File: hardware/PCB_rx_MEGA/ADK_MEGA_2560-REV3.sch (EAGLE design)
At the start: 9 parts

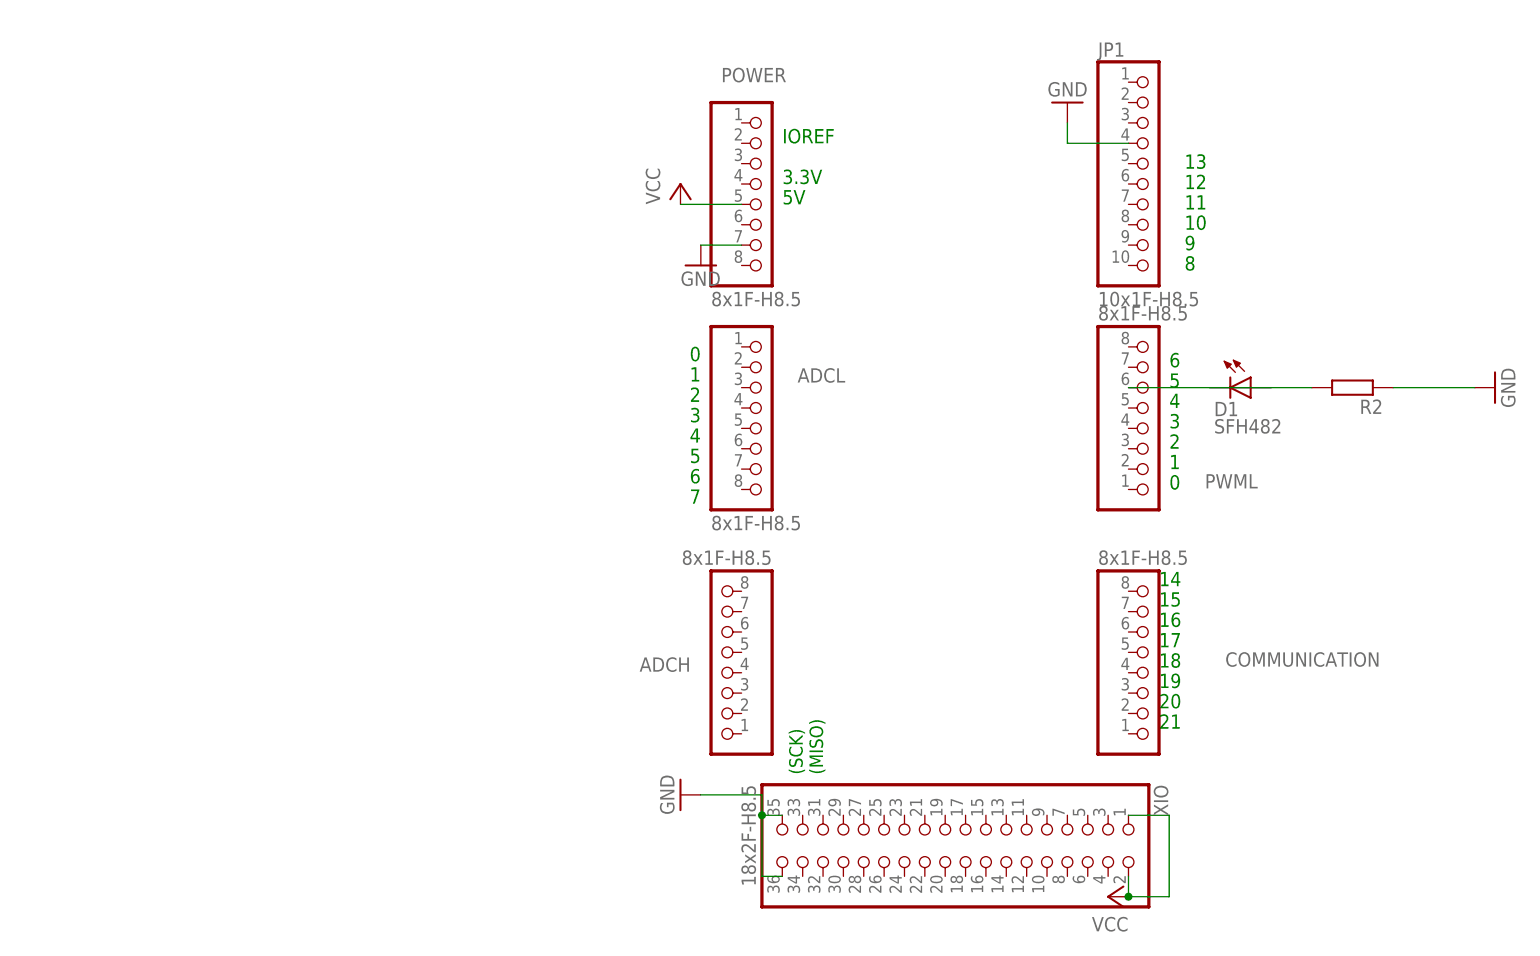
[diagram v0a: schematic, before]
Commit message: Se añade modulo de comunicaciones junto con regulador al diseño de la shield para el nodo central
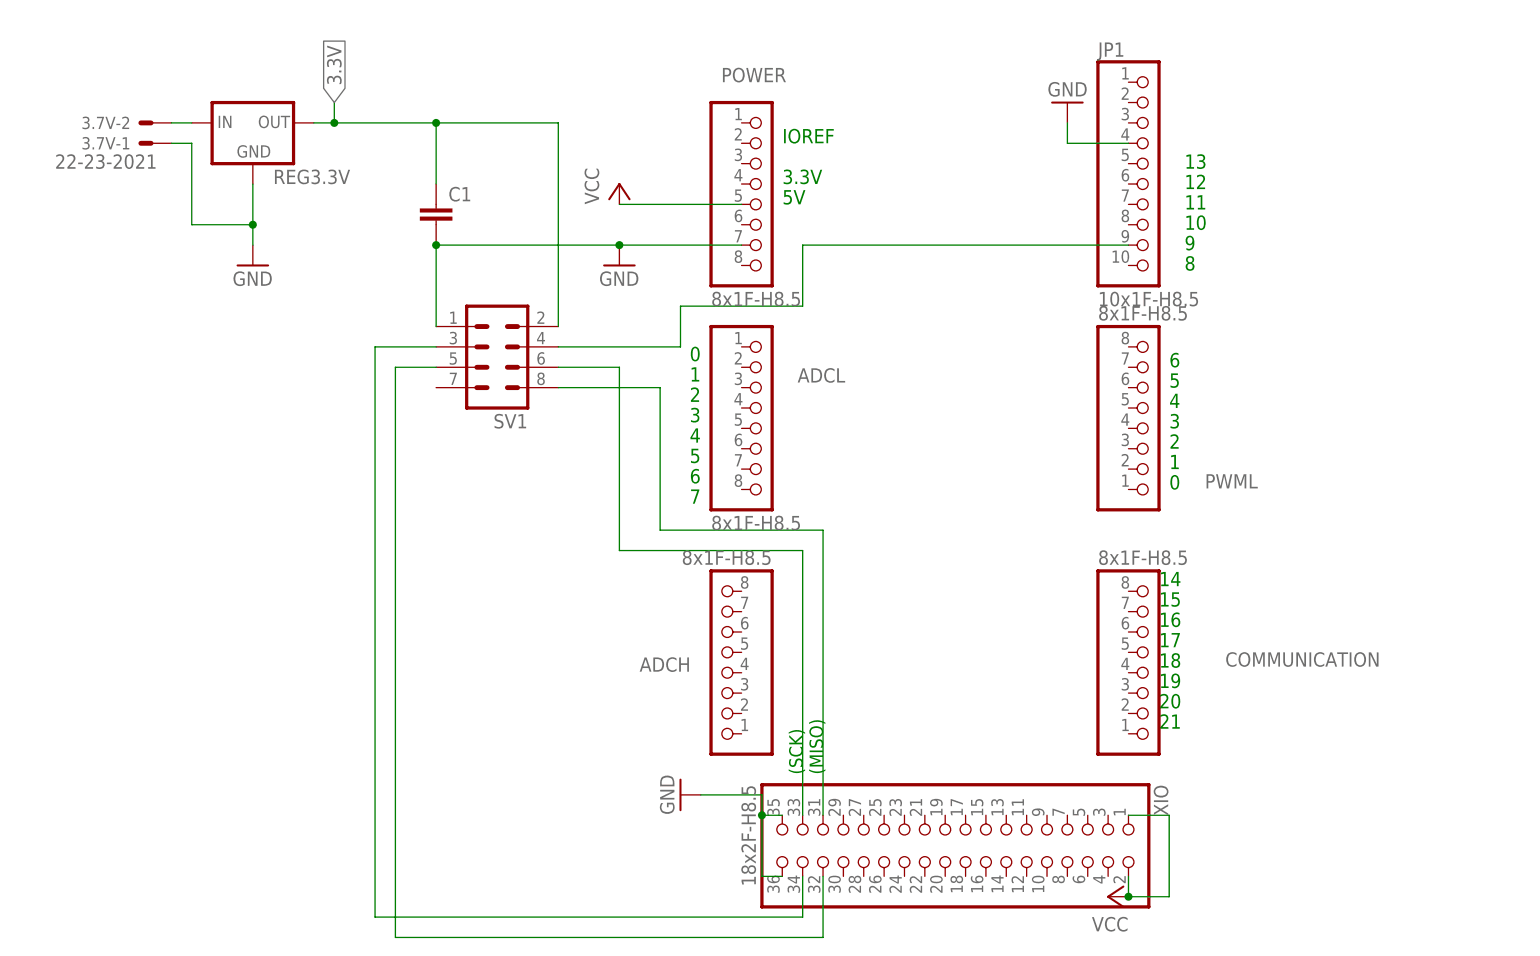
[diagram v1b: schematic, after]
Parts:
- removed D1: SFH482, led:SFH482
- removed R2: (no value), eagle-ltspice:R0204/7
- added 3.7V: 22-23-2021, con-molex:22-23-2021
- added C1: (no value), rcl:C-EU025-025X050
- added REG3.3V: (no value), v-reg:78XXL
- added SV1: (no value), con-lstb:MA04-2
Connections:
- removed net N$2: D1.C, PWML.6
- removed net N$3: D1.A, R2.2
- new net 3.3V: C1.1, REG3.3V.OUT, SV1.2
- new net N$1: SV1.3, XIO.34
- new net N$5: SV1.5, XIO.32
- new net N$6: JP1.9, SV1.4
- new net N$7: SV1.6, XIO.33
- new net N$8: SV1.8, XIO.31
- new net N$9: 3.7V-2.S, REG3.3V.IN
- net GND: now also 3.7V-1.S, C1.2, REG3.3V.GND, SV1.1; no longer R2.1
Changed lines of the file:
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@@
 <part name="JP1" library="SmartPrj" deviceset="PINHD-1X10" device="" value="10x1F-H8.5"/>
 <part name="POWER" library="SmartPrj" deviceset="PINHD-1X8" device="" value="8x1F-H8.5"/>
-<part name="R2" library="eagle-ltspice" deviceset="R" device="0204/7"/>
-<part name="D1" library="led" deviceset="SFH482" device=""/>
 <part name="GND1" library="supply1" deviceset="GND" device=""/>
 <part name="P+2" library="supply1" deviceset="VCC" device=""/>
-<part name="GND3" library="supply1" deviceset="GND" device=""/>
 <part name="P+12" library="supply1" deviceset="VCC" device=""/>
 <part name="GND13" library="supply1" deviceset="GND" device=""/>
 <part name="GND14" library="supply1" deviceset="GND" device=""/>
+<part name="SV1" library="con-lstb" deviceset="MA04-2" device=""/>
+<part name="C1" library="rcl" deviceset="C-EU" device="025-025X050"/>
+<part name="REG3.3V" library="v-reg" deviceset="78XXL" device=""/>
+<part name="GND2" library="supply1" deviceset="GND" device=""/>
+<part name="3.7V" library="con-molex" deviceset="22-23-2021" device=""/>
 </parts>
 <sheets>
@@
 <attribute name="VALUE" x="130.81" y="162.56" size="1.778" layer="96"/>
 </instance>
-<instance part="R2" gate="G$1" x="210.82" y="152.4" rot="R180"/>
-<instance part="D1" gate="1" x="198.12" y="152.4" rot="R270"/>
-<instance part="GND1" gate="1" x="129.54" y="167.64"/>
-<instance part="P+2" gate="VCC" x="127" y="177.8"/>
-<instance part="GND3" gate="1" x="228.6" y="152.4" rot="R90"/>
+<instance part="GND1" gate="1" x="119.38" y="167.64"/>
+<instance part="P+2" gate="VCC" x="119.38" y="177.8"/>
 <instance part="P+12" gate="VCC" x="180.34" y="88.9" rot="R90"/>
 <instance part="GND13" gate="1" x="127" y="101.6" rot="R270"/>
 <instance part="GND14" gate="1" x="175.26" y="187.96" rot="R180"/>
+<instance part="SV1" gate="G$1" x="104.14" y="154.94" rot="R180"/>
+<instance part="C1" gate="G$1" x="96.52" y="175.26"/>
+<instance part="REG3.3V" gate="A" x="73.66" y="185.42"/>
+<instance part="GND2" gate="1" x="73.66" y="167.64"/>
+<instance part="3.7V" gate="-1" x="60.96" y="182.88" rot="R180"/>
+<instance part="3.7V" gate="-2" x="60.96" y="185.42" rot="R180"/>
 </instances>
 <busses>
@@
 <segment>
 <pinref part="POWER" gate="A" pin="7"/>
-<wire x1="129.54" y1="170.18" x2="134.62" y2="170.18" width="0.1524" layer="91"/>
+<wire x1="119.38" y1="170.18" x2="134.62" y2="170.18" width="0.1524" layer="91"/>
 <pinref part="GND1" gate="1" pin="GND"/>
-</segment>
-<segment>
-<pinref part="R2" gate="G$1" pin="1"/>
-<pinref part="GND3" gate="1" pin="GND"/>
-<wire x1="226.06" y1="152.4" x2="215.9" y2="152.4" width="0.1524" layer="91"/>
+<pinref part="SV1" gate="G$1" pin="1"/>
+<wire x1="96.52" y1="160.02" x2="96.52" y2="170.18" width="0.1524" layer="91"/>
+<wire x1="96.52" y1="170.18" x2="119.38" y2="170.18" width="0.1524" layer="91"/>
+<junction x="119.38" y="170.18"/>
+<pinref part="C1" gate="G$1" pin="2"/>
+<junction x="96.52" y="170.18"/>
 </segment>
 <segment>
@@
 <wire x1="175.26" y1="182.88" x2="175.26" y2="185.42" width="0.1524" layer="91"/>
 </segment>
+<segment>
+<pinref part="REG3.3V" gate="A" pin="GND"/>
+<pinref part="GND2" gate="1" pin="GND"/>
+<wire x1="73.66" y1="170.18" x2="73.66" y2="172.72" width="0.1524" layer="91"/>
+<pinref part="3.7V" gate="-1" pin="S"/>
+<wire x1="73.66" y1="172.72" x2="73.66" y2="177.8" width="0.1524" layer="91"/>
+<wire x1="63.5" y1="182.88" x2="66.04" y2="182.88" width="0.1524" layer="91"/>
+<wire x1="66.04" y1="182.88" x2="66.04" y2="172.72" width="0.1524" layer="91"/>
+<wire x1="66.04" y1="172.72" x2="73.66" y2="172.72" width="0.1524" layer="91"/>
+<junction x="73.66" y="172.72"/>
+</segment>
 </net>
 <net name="VCC" class="0">
 <segment>
 <pinref part="POWER" gate="A" pin="5"/>
-<wire x1="127" y1="175.26" x2="134.62" y2="175.26" width="0.1524" layer="91"/>
+<wire x1="119.38" y1="175.26" x2="134.62" y2="175.26" width="0.1524" layer="91"/>
 <pinref part="P+2" gate="VCC" pin="VCC"/>
 </segment>
@@
 </segment>
 </net>
-<net name="N$2" class="0">
-<segment>
-<pinref part="PWML" gate="A" pin="6"/>
-<pinref part="D1" gate="1" pin="C"/>
-<wire x1="193.04" y1="152.4" x2="200.66" y2="152.4" width="0.1524" layer="91"/>
-<wire x1="193.04" y1="152.4" x2="182.88" y2="152.4" width="0.1524" layer="91"/>
-</segment>
-</net>
-<net name="N$3" class="0">
-<segment>
-<pinref part="R2" gate="G$1" pin="2"/>
-<pinref part="D1" gate="1" pin="A"/>
-<wire x1="200.66" y1="152.4" x2="205.74" y2="152.4" width="0.1524" layer="91"/>
-</segment>
-</net>
+<net name="N$1" class="0">
+<segment>
+<pinref part="SV1" gate="G$1" pin="3"/>
+<wire x1="96.52" y1="157.48" x2="88.9" y2="157.48" width="0.1524" layer="91"/>
+<wire x1="88.9" y1="157.48" x2="88.9" y2="86.36" width="0.1524" layer="91"/>
+<wire x1="88.9" y1="86.36" x2="142.24" y2="86.36" width="0.1524" layer="91"/>
+<pinref part="XIO" gate="A" pin="34"/>
+<wire x1="142.24" y1="86.36" x2="142.24" y2="91.44" width="0.1524" layer="91"/>
+</segment>
+</net>
+<net name="N$5" class="0">
+<segment>
+<pinref part="SV1" gate="G$1" pin="5"/>
+<wire x1="96.52" y1="154.94" x2="91.44" y2="154.94" width="0.1524" layer="91"/>
+<wire x1="91.44" y1="154.94" x2="91.44" y2="83.82" width="0.1524" layer="91"/>
+<pinref part="XIO" gate="A" pin="32"/>
+<wire x1="91.44" y1="83.82" x2="144.78" y2="83.82" width="0.1524" layer="91"/>
+<wire x1="144.78" y1="83.82" x2="144.78" y2="91.44" width="0.1524" layer="91"/>
+</segment>
+</net>
+<net name="N$6" class="0">
+<segment>
+<pinref part="JP1" gate="A" pin="9"/>
+<wire x1="182.88" y1="170.18" x2="142.24" y2="170.18" width="0.1524" layer="91"/>
+<wire x1="142.24" y1="170.18" x2="142.24" y2="162.56" width="0.1524" layer="91"/>
+<wire x1="142.24" y1="162.56" x2="127" y2="162.56" width="0.1524" layer="91"/>
+<wire x1="127" y1="162.56" x2="127" y2="157.48" width="0.1524" layer="91"/>
+<pinref part="SV1" gate="G$1" pin="4"/>
+<wire x1="127" y1="157.48" x2="111.76" y2="157.48" width="0.1524" layer="91"/>
+</segment>
+</net>
+<net name="N$7" class="0">
+<segment>
+<pinref part="SV1" gate="G$1" pin="6"/>
+<wire x1="111.76" y1="154.94" x2="119.38" y2="154.94" width="0.1524" layer="91"/>
+<wire x1="119.38" y1="154.94" x2="119.38" y2="132.08" width="0.1524" layer="91"/>
+<wire x1="119.38" y1="132.08" x2="142.24" y2="132.08" width="0.1524" layer="91"/>
+<pinref part="XIO" gate="A" pin="33"/>
+<wire x1="142.24" y1="132.08" x2="142.24" y2="99.06" width="0.1524" layer="91"/>
+</segment>
+</net>
+<net name="N$8" class="0">
+<segment>
+<pinref part="SV1" gate="G$1" pin="8"/>
+<wire x1="111.76" y1="152.4" x2="124.46" y2="152.4" width="0.1524" layer="91"/>
+<wire x1="124.46" y1="152.4" x2="124.46" y2="134.62" width="0.1524" layer="91"/>
+<pinref part="XIO" gate="A" pin="31"/>
+<wire x1="124.46" y1="134.62" x2="144.78" y2="134.62" width="0.1524" layer="91"/>
+<wire x1="144.78" y1="134.62" x2="144.78" y2="99.06" width="0.1524" layer="91"/>
+</segment>
+</net>
+<net name="N$9" class="0">
+<segment>
+<pinref part="REG3.3V" gate="A" pin="IN"/>
+<pinref part="3.7V" gate="-2" pin="S"/>
+<wire x1="66.04" y1="185.42" x2="63.5" y2="185.42" width="0.1524" layer="91"/>
+</segment>
+</net>
+<net name="3.3V" class="0">
+<segment>
+<pinref part="REG3.3V" gate="A" pin="OUT"/>
+<pinref part="C1" gate="G$1" pin="1"/>
+<wire x1="81.28" y1="185.42" x2="83.82" y2="185.42" width="0.1524" layer="91"/>
+<wire x1="83.82" y1="185.42" x2="96.52" y2="185.42" width="0.1524" layer="91"/>
+<wire x1="96.52" y1="185.42" x2="96.52" y2="177.8" width="0.1524" layer="91"/>
+<pinref part="SV1" gate="G$1" pin="2"/>
+<wire x1="96.52" y1="185.42" x2="111.76" y2="185.42" width="0.1524" layer="91"/>
+<wire x1="111.76" y1="185.42" x2="111.76" y2="160.02" width="0.1524" layer="91"/>
+<junction x="96.52" y="185.42"/>
+<label x="83.82" y="187.96" size="1.778" layer="95" rot="R90" xref="yes"/>
+<wire x1="83.82" y1="187.96" x2="83.82" y2="185.42" width="0.1524" layer="91"/>
+<junction x="83.82" y="185.42"/>
+</segment>
+</net>
